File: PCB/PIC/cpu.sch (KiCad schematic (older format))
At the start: 27 parts, among them P4 CONN_6, SW1 SW_PUSH_4, U16 PIC32MZ2048EC, U22 ASDMB-24.000MHZ-LC-T, U25 TC25L5I32K7680, U26 MCP9700

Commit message: elimino conector salida reles
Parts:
- C47, C48, C49, C50, C51, C52, C53, C54, C55, C56, C57, C58, C69, C82, C85: footprint ~ -> Capacitors_SMD:C_0603
- R100, R142, R90, R93, R94, R99: footprint ~ -> Resistors_SMD:R_0603
- SW1: footprint ~ -> (none)
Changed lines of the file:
@@
 encoding utf-8
 Sheet 11 13
-Title "CIAA-Microchip"
+Title "CPU"
 Date "16 feb 2016"
 Rev "1.0"
@@
 $EndDescr
 $Comp
-L GND-RESCUE-ciaa-pic #PWR0216
+L GND-RESCUE-ciaa-pic #PWR0215
 U 1 1 52C1CF47
 P 5300 9750
-F 0 "#PWR0216" H 5300 9750 30  0001 C CNN
+F 0 "#PWR0215" H 5300 9750 30  0001 C CNN
 F 1 "GND" H 5300 9680 30  0001 C CNN
 F 2 "" H 5300 9750 60  0000 C CNN
@@
 F 0 "C49" H 2600 10600 40  0000 L CNN
 F 1 "100nF" H 2606 10415 40  0000 L CNN
-F 2 "~" H 2638 10350 30  0000 C CNN
+F 2 "Capacitors_SMD:C_0603" H 2638 10350 30  0001 C CNN
 F 3 "~" H 2600 10500 60  0000 C CNN
 	1    2600 10500
@@
 F 0 "C50" H 2400 10600 40  0000 L CNN
 F 1 "10nF" H 2406 10415 40  0000 L CNN
-F 2 "~" H 2438 10350 30  0000 C CNN
+F 2 "Capacitors_SMD:C_0603" H 2438 10350 30  0001 C CNN
 F 3 "~" H 2400 10500 60  0000 C CNN
 	1    2400 10500
@@
 F 0 "C51" H 2200 10600 40  0000 L CNN
 F 1 "100nF" H 2206 10415 40  0000 L CNN
-F 2 "~" H 2238 10350 30  0000 C CNN
+F 2 "Capacitors_SMD:C_0603" H 2238 10350 30  0001 C CNN
 F 3 "~" H 2200 10500 60  0000 C CNN
 	1    2200 10500
@@
 F 0 "C52" H 2000 10600 40  0000 L CNN
 F 1 "10nF" H 2006 10415 40  0000 L CNN
-F 2 "~" H 2038 10350 30  0000 C CNN
+F 2 "Capacitors_SMD:C_0603" H 2038 10350 30  0001 C CNN
 F 3 "~" H 2000 10500 60  0000 C CNN
 	1    2000 10500
@@
 F 0 "C53" H 1800 10600 40  0000 L CNN
 F 1 "100nF" H 1806 10415 40  0000 L CNN
-F 2 "~" H 1838 10350 30  0000 C CNN
+F 2 "Capacitors_SMD:C_0603" H 1838 10350 30  0001 C CNN
 F 3 "~" H 1800 10500 60  0000 C CNN
 	1    1800 10500
@@
 F 0 "C54" H 1600 10600 40  0000 L CNN
 F 1 "10nF" H 1606 10415 40  0000 L CNN
-F 2 "~" H 1638 10350 30  0000 C CNN
+F 2 "Capacitors_SMD:C_0603" H 1638 10350 30  0001 C CNN
 F 3 "~" H 1600 10500 60  0000 C CNN
 	1    1600 10500
@@
 F 0 "C55" H 1400 10600 40  0000 L CNN
 F 1 "100nF" H 1406 10415 40  0000 L CNN
-F 2 "~" H 1438 10350 30  0000 C CNN
+F 2 "Capacitors_SMD:C_0603" H 1438 10350 30  0001 C CNN
 F 3 "~" H 1400 10500 60  0000 C CNN
 	1    1400 10500
@@
 F 0 "C56" H 1200 10600 40  0000 L CNN
 F 1 "10nF" H 1206 10415 40  0000 L CNN
-F 2 "~" H 1238 10350 30  0000 C CNN
+F 2 "Capacitors_SMD:C_0603" H 1238 10350 30  0001 C CNN
 F 3 "~" H 1200 10500 60  0000 C CNN
 	1    1200 10500
@@
 F 0 "C57" H 1000 10600 40  0000 L CNN
 F 1 "100nF" H 1006 10415 40  0000 L CNN
-F 2 "~" H 1038 10350 30  0000 C CNN
+F 2 "Capacitors_SMD:C_0603" H 1038 10350 30  0001 C CNN
 F 3 "~" H 1000 10500 60  0000 C CNN
 	1    1000 10500
@@
 F 0 "C58" H 800 10600 40  0000 L CNN
 F 1 "10nF" H 806 10415 40  0000 L CNN
-F 2 "~" H 838 10350 30  0000 C CNN
+F 2 "Capacitors_SMD:C_0603" H 838 10350 30  0001 C CNN
 F 3 "~" H 800 10500 60  0000 C CNN
 	1    800  10500
@@
 F 0 "C48" H 2800 10600 40  0000 L CNN
 F 1 "10nF" H 2806 10415 40  0000 L CNN
-F 2 "~" H 2838 10350 30  0000 C CNN
+F 2 "Capacitors_SMD:C_0603" H 2838 10350 30  0001 C CNN
 F 3 "~" H 2800 10500 60  0000 C CNN
 	1    2800 10500
@@
 F 0 "C47" H 3000 10600 40  0000 L CNN
 F 1 "100nF" H 3006 10415 40  0000 L CNN
-F 2 "~" H 3038 10350 30  0000 C CNN
+F 2 "Capacitors_SMD:C_0603" H 3038 10350 30  0001 C CNN
 F 3 "~" H 3000 10500 60  0000 C CNN
 	1    3000 10500
@@
 $EndComp
 $Comp
-L GND-RESCUE-ciaa-pic #PWR0217
+L GND-RESCUE-ciaa-pic #PWR0216
 U 1 1 52C1CF54
 P 600 11000
-F 0 "#PWR0217" H 600 11000 30  0001 C CNN
+F 0 "#PWR0216" H 600 11000 30  0001 C CNN
 F 1 "GND" H 600 10930 30  0001 C CNN
 F 2 "" H 600 11000 60  0000 C CNN
@@
 $EndComp
 $Comp
-L +3.3V-RESCUE-ciaa-pic #PWR0218
+L +3.3V-RESCUE-ciaa-pic #PWR0217
 U 1 1 52C1CF55
 P 3300 10100
-F 0 "#PWR0218" H 3300 10060 30  0001 C CNN
+F 0 "#PWR0217" H 3300 10060 30  0001 C CNN
 F 1 "+3.3V" H 3300 10210 30  0000 C CNN
 F 2 "" H 3300 10100 60  0000 C CNN
@@
 $EndComp
 $Comp
-L +3.3V-RESCUE-ciaa-pic #PWR0219
+L +3.3V-RESCUE-ciaa-pic #PWR0218
 U 1 1 52C1CF61
 P 1250 2850
-F 0 "#PWR0219" H 1250 2810 30  0001 C CNN
+F 0 "#PWR0218" H 1250 2810 30  0001 C CNN
 F 1 "+3.3V" H 1250 2960 30  0000 C CNN
 F 2 "" H 1250 2850 60  0000 C CNN
@@
 F 0 "C69" H 1250 3800 40  0000 L CNN
 F 1 "100nF" H 1256 3615 40  0000 L CNN
-F 2 "~" H 1288 3550 30  0000 C CNN
+F 2 "Capacitors_SMD:C_0603" H 1288 3550 30  0001 C CNN
 F 3 "~" H 1250 3700 60  0000 C CNN
 	1    1250 3700
@@
 $EndComp
 $Comp
-L GND-RESCUE-ciaa-pic #PWR0220
+L GND-RESCUE-ciaa-pic #PWR0219
 U 1 1 52C1CF63
 P 1250 4100
-F 0 "#PWR0220" H 1250 4100 30  0001 C CNN
+F 0 "#PWR0219" H 1250 4100 30  0001 C CNN
 F 1 "GND" H 1250 4030 30  0001 C CNN
 F 2 "" H 1250 4100 60  0000 C CNN
@@
 F 0 "R90" V 1330 3200 40  0000 C CNN
 F 1 "10K" V 1257 3201 40  0000 C CNN
-F 2 "~" V 1180 3200 30  0000 C CNN
+F 2 "Resistors_SMD:R_0603" V 1180 3200 30  0001 C CNN
 F 3 "~" H 1250 3200 30  0000 C CNN
 	1    1250 3200
@@
 F 0 "C82" H 900 1500 40  0000 L CNN
 F 1 "10nf" H 906 1315 40  0000 L CNN
-F 2 "~" H 938 1250 30  0000 C CNN
+F 2 "Capacitors_SMD:C_0603" H 938 1250 30  0001 C CNN
 F 3 "~" H 900 1400 60  0000 C CNN
 	1    900  1400
@@
 F 0 "R94" V 6980 9150 40  0000 C CNN
 F 1 "15K" V 6907 9151 40  0000 C CNN
-F 2 "~" V 6830 9150 30  0000 C CNN
+F 2 "Resistors_SMD:R_0603" V 6830 9150 30  0001 C CNN
 F 3 "~" H 6900 9150 30  0000 C CNN
 	1    6900 9150
@@
 $EndComp
 $Comp
-L GND-RESCUE-ciaa-pic #PWR0221
+L GND-RESCUE-ciaa-pic #PWR0220
 U 1 1 52C1CF70
 P 7000 9750
-F 0 "#PWR0221" H 7000 9750 30  0001 C CNN
+F 0 "#PWR0220" H 7000 9750 30  0001 C CNN
 F 1 "GND" H 7000 9680 30  0001 C CNN
 F 2 "" H 7000 9750 60  0000 C CNN
@@
 F 0 "R93" V 7180 9150 40  0000 C CNN
 F 1 "15K" V 7107 9151 40  0000 C CNN
-F 2 "~" V 7030 9150 30  0000 C CNN
+F 2 "Resistors_SMD:R_0603" V 7030 9150 30  0001 C CNN
 F 3 "~" H 7100 9150 30  0000 C CNN
 	1    7100 9150
@@
 F 0 "R99" V 3930 9300 40  0000 C CNN
 F 1 "2.2k" V 3857 9301 40  0000 C CNN
-F 2 "~" V 3780 9300 30  0000 C CNN
+F 2 "Resistors_SMD:R_0603" V 3780 9300 30  0001 C CNN
 F 3 "~" H 3850 9300 30  0000 C CNN
 	1    3850 9300
@@
 F 0 "R100" V 3730 9300 40  0000 C CNN
 F 1 "2.2k" V 3657 9301 40  0000 C CNN
-F 2 "~" V 3580 9300 30  0000 C CNN
+F 2 "Resistors_SMD:R_0603" V 3580 9300 30  0001 C CNN
 F 3 "~" H 3650 9300 30  0000 C CNN
 	1    3650 9300
@@
 $EndComp
 $Comp
-L +3.3V-RESCUE-ciaa-pic #PWR0222
+L +3.3V-RESCUE-ciaa-pic #PWR0221
 U 1 1 52C1CFA3
 P 3750 8850
-F 0 "#PWR0222" H 3750 8810 30  0001 C CNN
+F 0 "#PWR0221" H 3750 8810 30  0001 C CNN
 F 1 "+3.3V" H 3750 8960 30  0000 C CNN
 F 2 "" H 3750 8850 60  0000 C CNN
@@
 F 0 "R142" V 1980 3450 40  0000 C CNN
 F 1 "1K" V 1907 3451 40  0000 C CNN
-F 2 "~" V 1830 3450 30  0000 C CNN
+F 2 "Resistors_SMD:R_0603" V 1830 3450 30  0001 C CNN
 F 3 "~" H 1900 3450 30  0000 C CNN
 	1    1900 3450
@@
 PGEC2
 $Comp
-L GND-RESCUE-ciaa-pic #PWR0223
+L GND-RESCUE-ciaa-pic #PWR0222
 U 1 1 5398CB6F
 P 1700 6850
-F 0 "#PWR0223" H 1700 6850 30  0001 C CNN
+F 0 "#PWR0222" H 1700 6850 30  0001 C CNN
 F 1 "GND" H 1700 6780 30  0001 C CNN
 F 2 "" H 1700 6850 60  0000 C CNN
@@
 PGED2
 $Comp
-L GND-RESCUE-ciaa-pic #PWR0224
+L GND-RESCUE-ciaa-pic #PWR0223
 U 1 1 53A17893
 P 1050 9100
-F 0 "#PWR0224" H 1050 9100 30  0001 C CNN
+F 0 "#PWR0223" H 1050 9100 30  0001 C CNN
 F 1 "GND" H 1050 9030 30  0001 C CNN
 F 2 "" H 1050 9100 60  0000 C CNN
@@
 $EndComp
 $Comp
-L +3.3V-RESCUE-ciaa-pic #PWR0225
+L +3.3V-RESCUE-ciaa-pic #PWR0224
 U 1 1 53A17D5D
 P 2550 8400
-F 0 "#PWR0225" H 2550 8360 30  0001 C CNN
+F 0 "#PWR0224" H 2550 8360 30  0001 C CNN
 F 1 "+3.3V" H 2550 8510 30  0000 C CNN
 F 2 "" H 2550 8400 60  0000 C CNN
@@
 F 0 "C85" H 1750 8150 40  0000 L CNN
 F 1 "10nF" H 1756 7965 40  0000 L CNN
-F 2 "~" H 1788 7900 30  0000 C CNN
+F 2 "Capacitors_SMD:C_0603" H 1788 7900 30  0001 C CNN
 F 3 "~" H 1750 8050 60  0000 C CNN
 	1    1750 8050
@@
 GPIO15
 $Comp
-L +3.3V-RESCUE-ciaa-pic #PWR0226
+L +3.3V-RESCUE-ciaa-pic #PWR0225
 U 1 1 548AED7E
 P 1850 6950
-F 0 "#PWR0226" H 1850 6910 30  0001 C CNN
+F 0 "#PWR0225" H 1850 6910 30  0001 C CNN
 F 1 "+3.3V" H 1850 7060 30  0000 C CNN
 F 2 "" H 1850 6950 60  0000 C CNN
@@
 NoConn ~ 1200 1550
 $Comp
-L +3.3V-RESCUE-ciaa-pic #PWR0227
+L +3.3V-RESCUE-ciaa-pic #PWR0226
 U 1 1 548B0B5D
 P 900 1100
-F 0 "#PWR0227" H 900 1060 30  0001 C CNN
+F 0 "#PWR0226" H 900 1060 30  0001 C CNN
 F 1 "+3.3V" H 900 1210 30  0000 C CNN
 F 2 "" H 900 1100 60  0000 C CNN
@@
 $EndComp
 $Comp
-L GND-RESCUE-ciaa-pic #PWR0228
+L GND-RESCUE-ciaa-pic #PWR0227
 U 1 1 548B1668
 P 900 2150
-F 0 "#PWR0228" H 900 2150 30  0001 C CNN
+F 0 "#PWR0227" H 900 2150 30  0001 C CNN
 F 1 "GND" H 900 2080 30  0001 C CNN
 F 2 "" H 900 2150 60  0000 C CNN
@@
 $EndComp
 $Comp
-L GND-RESCUE-ciaa-pic #PWR0229
+L GND-RESCUE-ciaa-pic #PWR0228
 U 1 1 551AD1DE
 P 1350 5950
-F 0 "#PWR0229" H 1350 5950 30  0001 C CNN
+F 0 "#PWR0228" H 1350 5950 30  0001 C CNN
 F 1 "GND" H 1350 5880 30  0001 C CNN
 F 2 "" H 1350 5950 60  0000 C CNN
@@
 $EndComp
 $Comp
-L +3.3V-RESCUE-ciaa-pic #PWR0230
+L +3.3V-RESCUE-ciaa-pic #PWR0229
 U 1 1 551AD1E4
 P 1200 4850
-F 0 "#PWR0230" H 1200 4810 30  0001 C CNN
+F 0 "#PWR0229" H 1200 4810 30  0001 C CNN
 F 1 "+3.3V" H 1200 4960 30  0000 C CNN
 F 2 "" H 1200 4850 60  0000 C CNN
@@
 F 0 "SW1" H 1050 3650 50  0000 C CNN
 F 1 "SW_PUSH_4" H 1050 3900 50  0000 C CNN
-F 2 "~" H 1050 3750 60  0000 C CNN
+F 2 "" H 1050 3750 60  0001 C CNN
 F 3 "~" H 1050 3750 60  0000 C CNN
 	1    1050 3750
@@
 S. Tempetura
 $Comp
-L +3.3V-RESCUE-ciaa-pic #PWR0231
+L +3.3V-RESCUE-ciaa-pic #PWR0230
 U 1 1 575B8473
 P 4800 800
-F 0 "#PWR0231" H 4800 760 30  0001 C CNN
+F 0 "#PWR0230" H 4800 760 30  0001 C CNN
 F 1 "+3.3V" H 4800 910 30  0000 C CNN
 F 2 "" H 4800 800 60  0000 C CNN
@@
 $EndComp
 $Comp
-L +3.3VADC #PWR0232
+L +3.3VADC #PWR0231
 U 1 1 575BA482
 P 5550 800
-F 0 "#PWR0232" H 5550 920 20  0001 C CNN
+F 0 "#PWR0231" H 5550 920 20  0001 C CNN
 F 1 "+3.3VADC" H 5550 890 30  0000 C CNN
 F 2 "" H 5550 800 60  0000 C CNN

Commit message: rev02 aignacion footprint
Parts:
- SW1: footprint (none) -> footprints:PUSH_SWITCH
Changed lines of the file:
@@
 F 0 "SW1" H 1050 3650 50  0000 C CNN
 F 1 "SW_PUSH_4" H 1050 3900 50  0000 C CNN
-F 2 "" H 1050 3750 60  0001 C CNN
+F 2 "footprints:PUSH_SWITCH" H 1050 3750 60  0001 C CNN
 F 3 "~" H 1050 3750 60  0000 C CNN
 	1    1050 3750

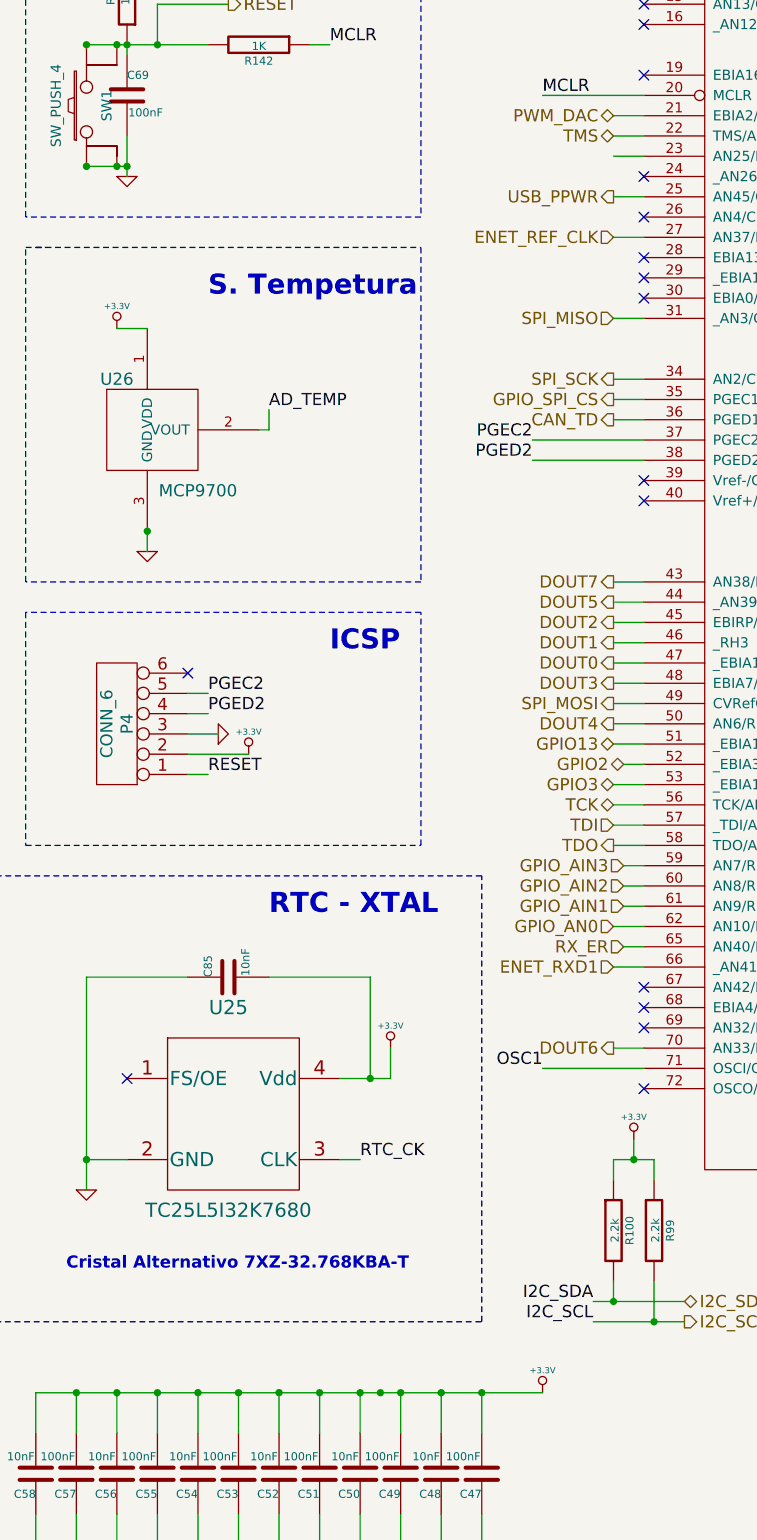
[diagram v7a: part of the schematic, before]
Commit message: rev02 se completa campo num. de frabicante(manf#) CIAA-PIC
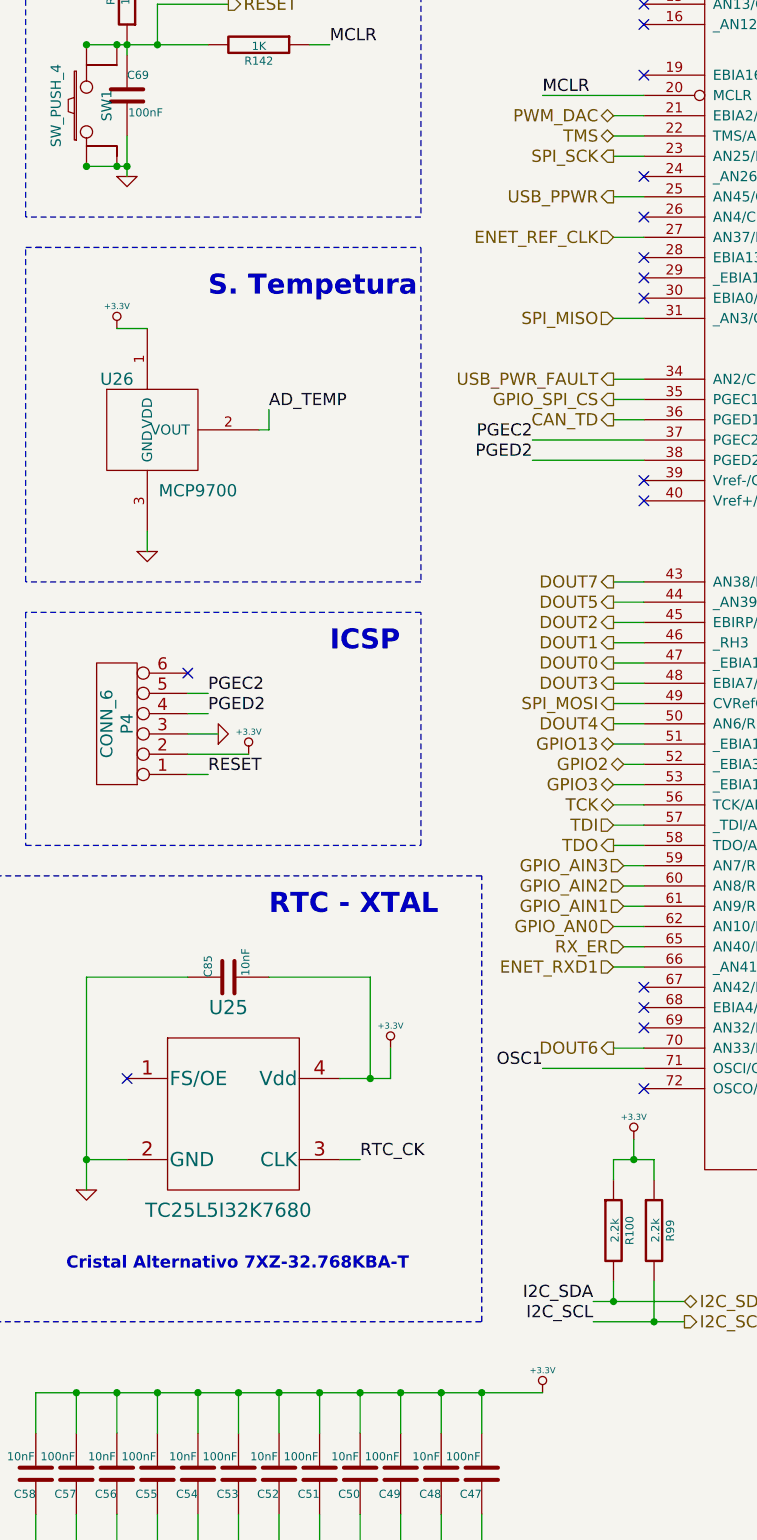
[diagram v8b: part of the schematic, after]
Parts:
- SW1: manf# (none) -> FSM2JSMAATR
- U16: manf# (none) -> PIC32MZ2048ECH144-I/PL
- U22: manf# (none) -> ASDMB-24.000MHZ-LC-T
- U25: manf# (none) -> TC25L5I32K7680
- U26: manf# (none) -> MCP9700AT-E/TT
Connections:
- net SPI_SCK: now also U16.23 (AN25/RPE8/RE8); no longer U16.34 (AN2/C2INB/RPB2/RB2)
- new net USB_PWR_FAULT: U16.34 (AN2/C2INB/RPB2/RB2)
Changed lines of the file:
@@
 Text HLabel 3650 5300 0    60   Output ~ 0
 CAN_TD
-Text HLabel 3650 5100 0    60   Output ~ 0
+Text HLabel 3650 4000 0    60   Output ~ 0
 SPI_SCK
 Text HLabel 3650 3150 0    60   Output ~ 0
@@
 F 2 "footprints:LQFP144-M05" H 5300 350 60  0001 C CNN
 F 3 "http://ww1.microchip.com/downloads/en/DeviceDoc/60001191E.pdf" H 5300 200 60  0001 C CNN
+F 4 "PIC32MZ2048ECH144-I/PL" H 5300 5250 60  0001 C CNN "manf#"
 	1    5300 5250
 	1    0    0    -1
@@
 F 2 "footprints:4SMD" H 1750 8200 60  0001 C CNN
 F 3 "http://www.digikey.com/product-detail/es/cts-frequency-controls/TC25L5I32K7680/CTX1183CT-ND/3511747" H 800 10050 60  0001 C CNN
+F 4 "TC25L5I32K7680" H 1750 8750 60  0001 C CNN "manf#"
 	1    1750 8750
 	1    0    0    -1
@@
 F 2 "footprints:SOT23" H 2000 4850 60  0001 C CNN
 F 3 "http://www.digikey.com/product-detail/es/microchip-technology/MCP9700AT-E-TT/MCP9700AT-E-TTCT-ND/3622388" H 3450 50  60  0001 C CNN
+F 4 "MCP9700AT-E/TT" H 1350 5350 60  0001 C CNN "manf#"
 	1    1350 5350
 	1    0    0    -1
@@
 F 2 "footprints:PUSH_SWITCH" H 1050 3750 60  0001 C CNN
 F 3 "~" H 1050 3750 60  0000 C CNN
+F 4 "FSM2JSMAATR" H 1050 3750 60  0001 C CNN "manf#"
 	1    1050 3750
 	0    -1   -1   0
@@
 F 2 "footprints:4SMD" H 1700 1200 60  0001 C CNN
 F 3 "http://www.digikey.com/product-detail/es/abracon-llc/ASDMB-24.000MHZ-LC-T/535-11728-1-ND/2809937" H 3200 2900 60  0001 C CNN
+F 4 "ASDMB-24.000MHZ-LC-T" H 1700 1750 60  0001 C CNN "manf#"
 	1    1700 1750
 	1    0    0    -1
@@
 	3650 4200 3800 4200
 Wire Wire Line
-	3650 4000 3800 4000
-Wire Wire Line
 	3650 7100 3800 7100
 Wire Wire Line
@@
 Connection ~ 2200 10100
 Connection ~ 2400 10100
-Connection ~ 2500 10100
 Wire Wire Line
 	4650 9300 4650 9550
@@
 Wire Wire Line
 	3800 7000 3700 7000
-Connection ~ 1350 5850
 Connection ~ 1050 8950
 Connection ~ 1050 3450
@@
 Wire Wire Line
 	3650 7400 3800 7400
+Wire Wire Line
+	3650 4000 3800 4000
+Text HLabel 3650 5100 0    60   Output ~ 0
+USB_PWR_FAULT
 $EndSCHEMATC
